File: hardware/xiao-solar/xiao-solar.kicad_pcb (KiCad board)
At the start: 2 copper layers, 48 x 86 mm, 84 parts, among them J1 SOLAR, J2 VIN2 5-20V, J3 NTC 10k (103AT), J4 BATTERY, J5 I2C rail, J6 LOAD_IN до 12V, J7 OUT1 heater, J8 OUT2 fan, J9 OUT3 spare, Q1 AO3400A, Q2 AO3400A (ship FET), Q3 FS8205A, Q4 AO3400A, Q5 AO3400A, Q6 AO3400A, Q7 AO3401A, U1 BQ25798RQMR, U2 DW01A, U3 XIAO nRF52840, U4 Wio-SX1262 for XIAO, U5 SHT40-AD1B, U6 PCA9685PW

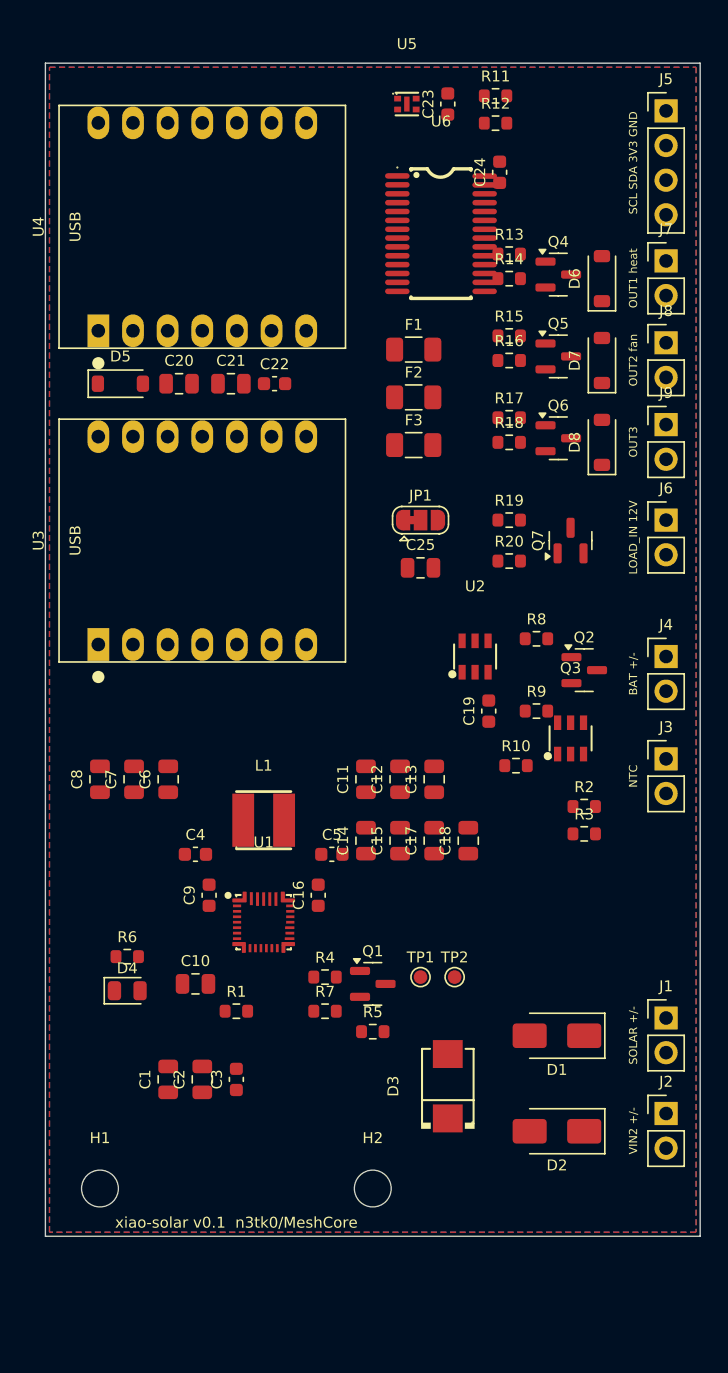
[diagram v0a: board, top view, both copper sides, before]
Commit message: xiao-solar v0.2 WIP: Argon review fixes, layout and first routing
- CE straight on D0, JP2 selects pull-down (Li-ion, charges without the Xiao) or
  pull-up (LiFePO4, charges only after firmware set VREG); Q1/R5 removed
- VBUS/PMID caps 10uF/50V 1206; SMBJ24A and HJ8205 swapped to preferred parts
- charger laid out per the BQ25798 layout guide, TS divider and side-pin parts at U1,
  GND pin 27 runs under the package to pins 10/11 and a via
- SHT40 on a slotted tongue without copper pour
- LOAD_IN removed; loads on SYS through an LC filter (2.2uH + 2x22uF), PGND with a
  net tie, 1k gate resistors and 100nF across each output against radio noise
- four 2.8 mm mounting holes with 6 mm keepout, board 48x94 mm
- tools/route.py (Freerouting + SES import + GND stitching), refill.py, finish.py,
  export.py (Gerber/drill zip, JLC CPL); __pycache__ removed, .gitignore added
- 3 connections still unrouted (QON, BTST2, PWM1)

Co-Authored-By: Claude Opus 5.5 <noreply@anthropic.com>
Claude-Session: https://claude.ai/code/session_01P5Km81NY9NPL6RpKFGVEbH
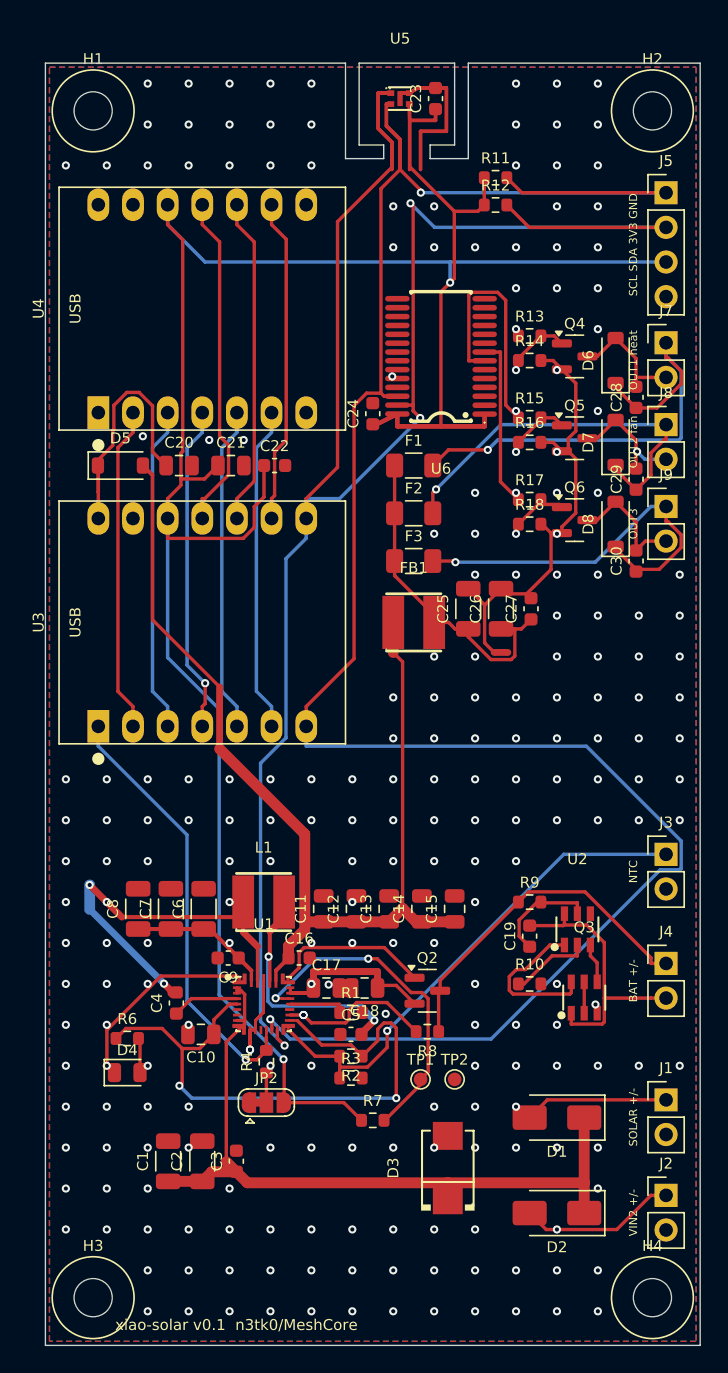
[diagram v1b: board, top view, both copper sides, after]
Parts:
- removed J6: LOAD_IN до 12V, Connector_PinHeader_2.54mm:PinHeader_1x02_P2.54mm_Vertical
- removed JP1: VLOAD: 1-2 SYS / 2-3 LOAD_IN, Jumper:SolderJumper-3_P1.3mm_Bridged12_RoundedPad1.0x1.5mm
- removed Q1: AO3400A, Package_TO_SOT_SMD:SOT-23
- removed Q7: AO3401A, Package_TO_SOT_SMD:SOT-23
- removed R19: 22k, Resistor_SMD:R_0603_1608Metric
- removed R20: 10k, Resistor_SMD:R_0603_1608Metric
- removed R5: 100k, Resistor_SMD:R_0603_1608Metric
- added C26: 22u/25V, Capacitor_SMD:C_1206_3216Metric, F.Cu at (133.4, 140.0)
- added C27: 100n, Capacitor_SMD:C_0603_1608Metric, F.Cu at (135.6, 140.0)
- added C28: 100n, Capacitor_SMD:C_0603_1608Metric, F.Cu at (143.3, 124.5)
- added C29: 100n, Capacitor_SMD:C_0603_1608Metric, F.Cu at (143.3, 130.5)
- added C30: 100n, Capacitor_SMD:C_0603_1608Metric, F.Cu at (143.3, 136.5)
- added FB1: 2.2uH 3.2A, xiao_solar:IND-SMD_L4.0-W4.0_FNR40XXS, F.Cu at (127.0, 141.0)
- added H3: M2/M2.5, xiao_solar:MountingHole_2.8mm_Keepout6mm, F.Cu at (103.5, 190.5)
- added H4: M2/M2.5, xiao_solar:MountingHole_2.8mm_Keepout6mm, F.Cu at (144.5, 190.5)
- added JP2: CE: 1-2 Li-ion / 2-3 LiFePO4, Jumper:SolderJumper-3_P1.3mm_Bridged12_RoundedPad1.0x1.5mm, F.Cu at (116.2, 176.2)
- added NT1: PGND-GND, NetTie:NetTie-2_SMD_Pad0.5mm, F.Cu at (133.4, 143.2)
- C1, C2, C6, C7, C8: value 10u/25V -> 10u/50V; footprint Capacitor_SMD:C_0805_2012Metric -> Capacitor_SMD:C_1206_3216Metric
- C25: value 10u/25V -> 22u/25V; footprint Capacitor_SMD:C_0805_2012Metric -> Capacitor_SMD:C_1206_3216Metric
- H1, H2: value M2.5 -> M2/M2.5; footprint MountingHole:MountingHole_2.7mm_M2.5 -> xiao_solar:MountingHole_2.8mm_Keepout6mm
- Q3: value FS8205A -> HJ8205
- R13, R15, R17: value 100 -> 1k
- moved H2 81.6 mm to (144.5, 103.5)
- moved H1 79.0 mm to (103.5, 103.5)
- moved R8 29.9 mm to (128.0, 171.0), turned to 180 degrees
- moved Q2 26.2 mm to (128.0, 168.0)
- moved R2 25.0 mm to (122.4, 172.8), turned to 180 degrees
- moved R3 24.8 mm to (122.4, 174.4)
- moved J4 22.5 mm to (145.5, 166.0)
- moved U2 21.4 mm to (139.0, 163.5)
- moved C24 20.0 mm to (124.0, 125.7)
- moved Q3 19.0 mm to (139.5, 168.5)
- moved C19 16.8 mm to (135.5, 164.0)
- moved R10 16.0 mm to (135.5, 167.5)
- moved R9 14.0 mm to (135.5, 161.5)
- moved C17 13.4 mm to (120.6, 167.8), turned to 0 degrees
- moved C5 13.3 mm to (122.4, 171.2)
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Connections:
- C25 pad 2: GND -> PGND
- Q4 pad 2: GND -> PGND
- Q5 pad 2: GND -> PGND
- Q6 pad 2: GND -> PGND
- R14 pad 2: GND -> PGND
- R16 pad 2: GND -> PGND
- R18 pad 2: GND -> PGND
- R4 pad 1: REGN -> CE_PULL
- U3 pad 1: CHG_EN -> CE
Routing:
- net 3V3: track 0.00 -> 194.2 mm, vias 0 -> 2
- net SCL: track 0.00 -> 159.7 mm, vias 0 -> 2
- net SDA: track 0.00 -> 145.6 mm, vias 0 -> 3
- net SYS: track 0.00 -> 76.6 mm
- net VBUS: track 0.00 -> 55.3 mm
- net REGN: track 0.00 -> 46.6 mm, vias 0 -> 2
- net TS: track 0.00 -> 37.3 mm, vias 0 -> 1
- net OUT1+: track 0.00 -> 36.6 mm, vias 0 -> 1
- net GND: track 0.00 -> 34.2 mm, vias 0 -> 212
- net PGND: track 0.00 -> 34.1 mm, vias 0 -> 3
- net CE: track 0.00 -> 32.2 mm, vias 0 -> 1
- net SW1: track 0.00 -> 29.1 mm, vias 0 -> 4
- net OUT2+: track 0.00 -> 28.9 mm, vias 0 -> 1
- net OUT3+: track 0.00 -> 28.8 mm, vias 0 -> 1
- net BATT+: track 0.00 -> 25.5 mm
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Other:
- board size 48 x 86 mm -> 48 x 94 mm
- board text removed: "LOAD_IN 12V"

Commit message: xiao-solar v0.2: final routing, Gerber, JLC BOM/CPL
CE jumper JP2 (Li-ion/LiFePO4), INT left open, 4 mounting holes 2.8 mm
with 6 mm keep-out, LOAD_IN removed, load noise filtering (LC on VLOAD,
PGND star via net tie, 1k gates, 100n per output), fewer JLC extended
parts. Routing tools: finish.py second pass, patch_route.py grid A*.
DRC: 0 unconnected, only net-tie polygon clearance and cosmetic items.

Co-Authored-By: Claude Opus 5.5 <noreply@anthropic.com>
Claude-Session: https://claude.ai/code/session_01P5Km81NY9NPL6RpKFGVEbH
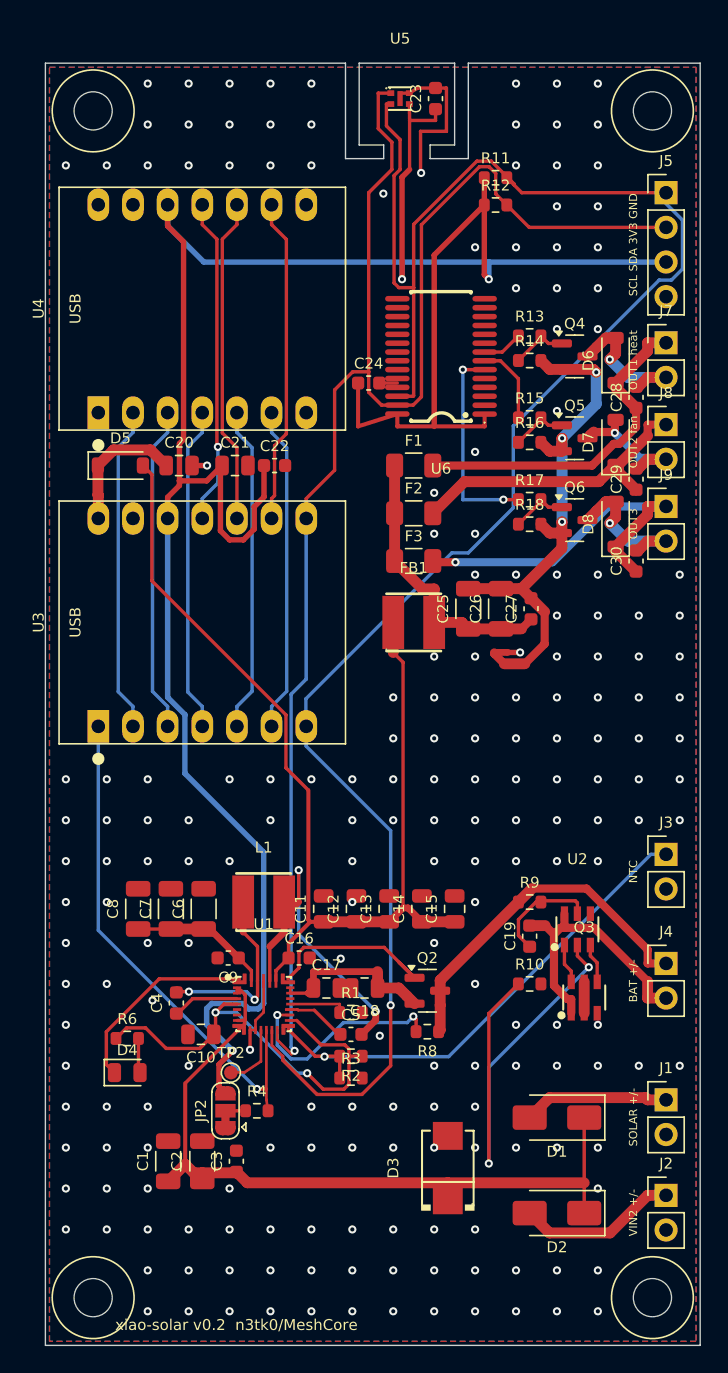
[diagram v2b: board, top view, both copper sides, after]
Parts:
- removed R7: 10k, Resistor_SMD:R_0603_1608Metric
- removed TP1: INT, TestPoint:TestPoint_Pad_D1.0mm
- moved TP2 16.4 mm to (113.6, 174.0)
- moved R4 3.67 mm to (115.5, 176.8), turned to 0 degrees
- moved JP2 3.06 mm to (113.2, 176.8), turned to 90 degrees
- moved C24 2.27 mm to (123.7, 123.5), turned to 0 degrees
- moved C21 0.30 mm to (113.9, 129.5)
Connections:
- U1 pad 21: INT -> (no net)
- U6 pad 6: PWM1 -> PWM3
- U6 pad 8: PWM3 -> PWM1
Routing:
- net DW_CS: track 5.97 -> 33.5 mm, vias 0 -> 2
- net SDA: track 145.6 -> 118.9 mm, vias 3 -> 1
- net INT: track 25.0 -> 0.00 mm, vias 2 -> 0
- net SCL: track 159.7 -> 143.7 mm, vias 2 -> 1
- net SW1: track 29.1 -> 13.7 mm, vias 4 -> 2
- net GND: track 34.2 -> 20.4 mm, vias 212 -> 205
- net REGN: track 46.6 -> 33.1 mm
- net PWM2: track 18.0 -> 5.88 mm, vias 1 -> 0
- net OUT1+: track 36.6 -> 25.2 mm, vias 1 -> 0
- net XIAO_5V: track 19.3 -> 9.84 mm
- net DW_OD: track 11.5 -> 2.91 mm
- net BAT: track 22.0 -> 13.7 mm, vias 1 -> 0
- net PGND: track 34.1 -> 40.9 mm
- net OUT2+: track 28.9 -> 22.6 mm, vias 1 -> 0
- net 3V3: track 194.2 -> 188.2 mm, vias 2 -> 3
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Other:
- board text added: "xiao-solar v0.2 n3tk0/MeshCore"
- board text removed: "xiao-solar v0.1 n3tk0/MeshCore"

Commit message: hardware: charger zone per BQ25798 layout guide, v0.3 of both boards
- tools/charger.py: shared BQ25798 cluster (placement, PMID/SYS/VBUS/BAT/SW
  copper zones, hand routes) for xiao-solar and xiao-solar-lite
- 100 nF PMID/SYS caps at the pins, SW short and wide to L1, BTST/REGN/GND
  through vias under the package, BAT halves joined on B.Cu
- lite: TI cap counts (VBUS 2, PMID 3, SYS 5), 23 x 57 mm, D5 fed from SYS
- thermal spokes on small parts, solid on charger power caps
- routing: zone copper goes to Freerouting as fixed hatched wires, locked
  hand routes survive the finish pass; JLC CPL rotation fix for SOT-23/LED
- both boards 0 unconnected; READMEs, Gerber, BOM, CPL, PDFs, images

Co-Authored-By: Claude Opus 5.5 <noreply@anthropic.com>
Claude-Session: https://claude.ai/code/session_01P5Km81NY9NPL6RpKFGVEbH
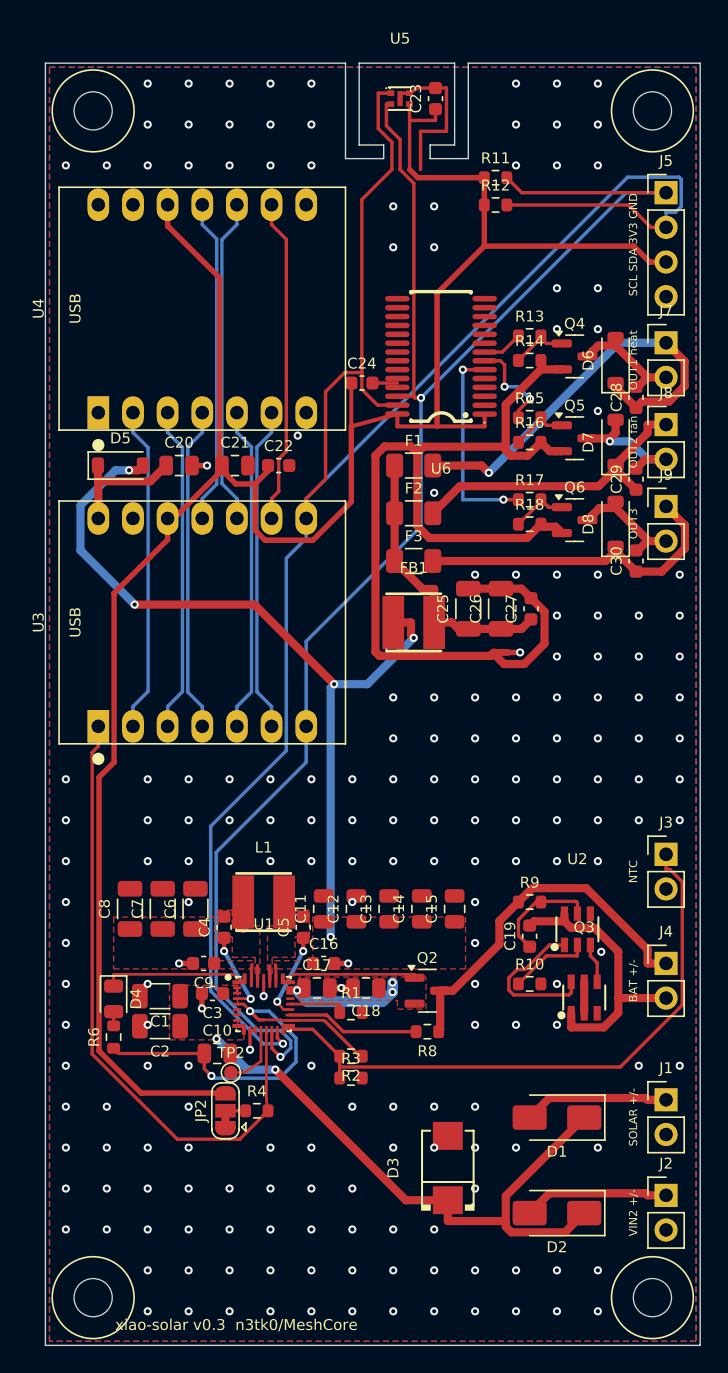
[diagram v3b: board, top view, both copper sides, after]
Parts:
- moved C3 12.4 mm to (112.2, 168.2), turned to 180 degrees
- moved C1 12.1 mm to (108.4, 168.4), turned to 180 degrees
- moved C2 10.4 mm to (108.4, 170.6), turned to 180 degrees
- moved C5 8.59 mm to (118.9, 163.3), turned to 90 degrees
- moved C4 6.56 mm to (113.1, 163.3)
- moved D4 5.49 mm to (105.0, 168.6), turned to -90 degrees
- moved C16 1.84 mm to (120.4, 166.0)
- moved C9 1.84 mm to (111.6, 166.0)
- moved C10 1.84 mm to (112.6, 172.6), turned to 0 degrees
- moved R6 1.00 mm to (105.0, 171.4), turned to 90 degrees
- moved C17 0.70 mm to (119.9, 167.8)
- moved C7 0.60 mm to (108.6, 162.0)
- moved C6 0.60 mm to (111.0, 162.0)
- moved C8 0.60 mm to (106.2, 162.0)
- moved C24 0.50 mm to (123.2, 123.5)
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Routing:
- net PGND: track 40.9 -> 78.4 mm, vias 3 -> 0
- net DW_CS: track 33.5 -> 5.97 mm, vias 2 -> 0
- net 3V3: track 188.2 -> 162.1 mm, vias 3 -> 0
- net SDA: track 118.9 -> 141.4 mm
- net SCL: track 143.7 -> 121.3 mm, vias 1 -> 2
- net SW2: track 24.9 -> 2.99 mm, vias 2 -> 0
- net SYS: track 76.6 -> 61.3 mm, vias 0 -> 5
- net VBUS: track 56.5 -> 44.9 mm, vias 0 -> 2
- net SW1: track 13.7 -> 2.99 mm, vias 2 -> 0
- net PMID: track 10.3 -> 1.15 mm
- net DW_OD: track 2.91 -> 11.6 mm
- net CE: track 38.0 -> 46.5 mm, vias 1 -> 0
- net TS: track 37.4 -> 44.9 mm, vias 1 -> 0
- net OUT1+: track 25.2 -> 31.7 mm, vias 0 -> 1
- net BATP: track 16.0 -> 9.76 mm, vias 2 -> 0
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- added copper zone on F.Cu, net BAT
- added copper zone on F.Cu, net PMID
- added copper zone on F.Cu, net SW1
- added copper zone on F.Cu, net SW2
- added copper zone on F.Cu, net SYS
- added copper zone on F.Cu, net VBUS
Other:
- board text added: "xiao-solar v0.3 n3tk0/MeshCore"
- board text removed: "xiao-solar v0.2 n3tk0/MeshCore"

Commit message: hardware: two vias per power layer change, no vias in pads
- BAT halves joined on B.Cu with two vias at each end (C17/C18/Q2 moved)
- refill.py: second via next to every power-net via that is alone
- lite: VBUS from the input diodes as one 0.8 mm B.Cu run, two vias at
  each end; main: fixed landing vias for the VBUS bus in the VBUS copper
- stitching/island vias stay off pads (kicad-happy VP-001 findings)
- main: own GND via for C22 between the module rows
- Gerber, BOM, CPL, PDFs and images regenerated; both boards 0 unconnected

Co-Authored-By: Claude Opus 5.5 <noreply@anthropic.com>
Claude-Session: https://claude.ai/code/session_01P5Km81NY9NPL6RpKFGVEbH
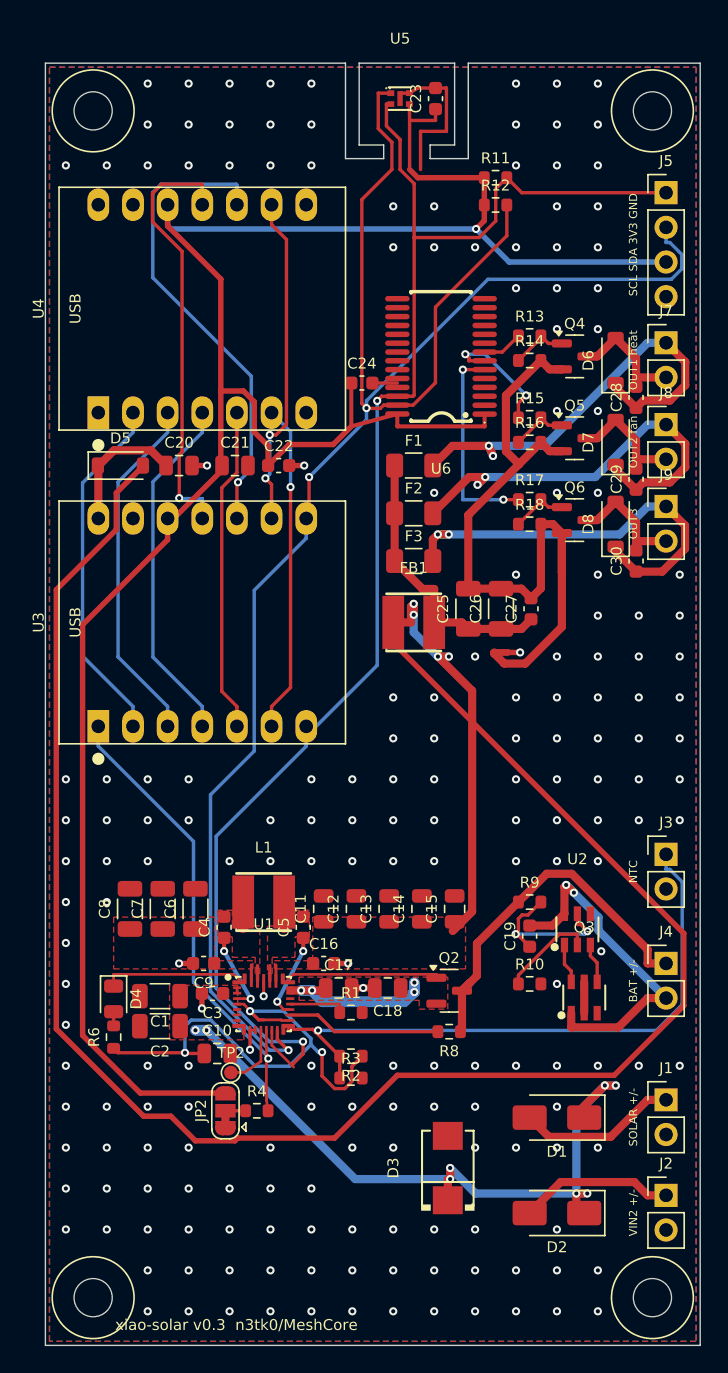
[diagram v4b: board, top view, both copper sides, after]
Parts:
- moved C17 1.60 mm to (121.5, 167.8)
- moved C18 1.60 mm to (125.1, 167.8)
- moved Q2 1.60 mm to (129.6, 168.0)
- moved R8 1.60 mm to (129.6, 171.0)
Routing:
- net SYS: track 61.3 -> 167.0 mm, vias 5 -> 4
- net PGND: track 78.4 -> 54.3 mm
- net SCL: track 121.3 -> 109.6 mm
- net SPI_MISO: track 23.9 -> 35.2 mm, vias 0 -> 1
- net CE: track 46.5 -> 35.6 mm, vias 0 -> 1
- net OUT2+: track 22.5 -> 31.8 mm, vias 0 -> 2
- net DW_OD: track 11.6 -> 2.91 mm
- net SPI_MOSI: track 23.9 -> 31.9 mm, vias 0 -> 1
- net VBUS: track 44.9 -> 52.8 mm, vias 2 -> 8
- net OUT3+: track 24.1 -> 31.7 mm, vias 0 -> 2
- net SDA: track 141.4 -> 134.7 mm, vias 1 -> 3
- net REGN: track 32.1 -> 38.1 mm, vias 2 -> 3
- net BATT-: track 21.0 -> 26.9 mm, vias 0 -> 2
- net 3V3: track 162.1 -> 165.9 mm, vias 0 -> 1
- net DW_VCC: track 8.04 -> 11.9 mm, vias 0 -> 2
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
